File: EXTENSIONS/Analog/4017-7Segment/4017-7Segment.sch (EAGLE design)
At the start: 19 parts

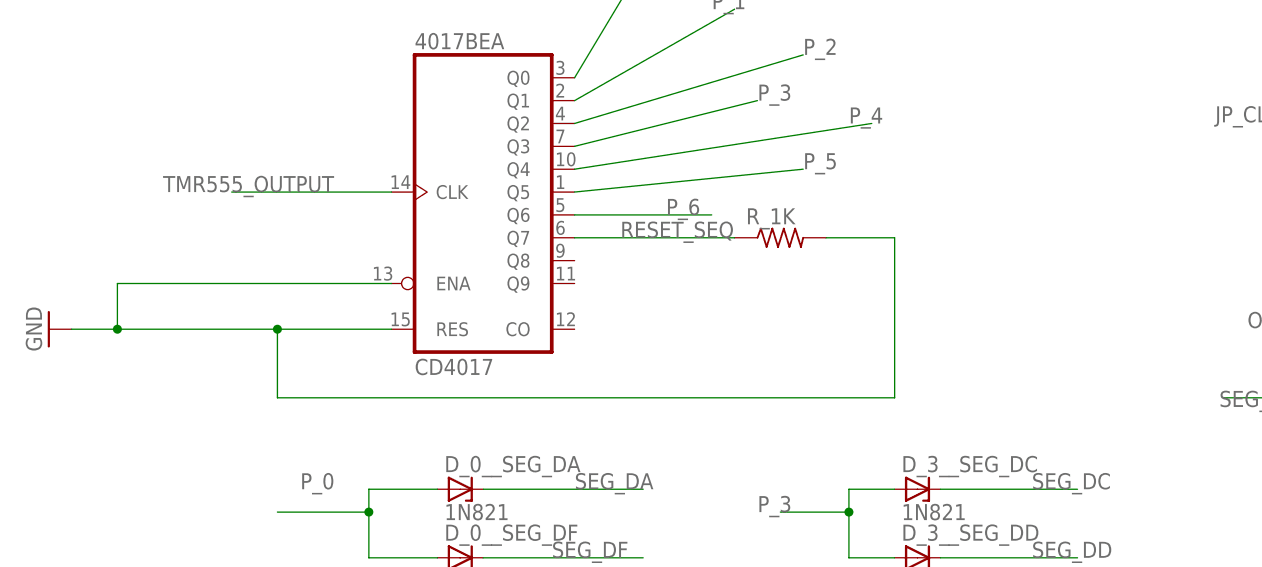
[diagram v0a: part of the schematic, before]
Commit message: Created 4017-7Segment v2
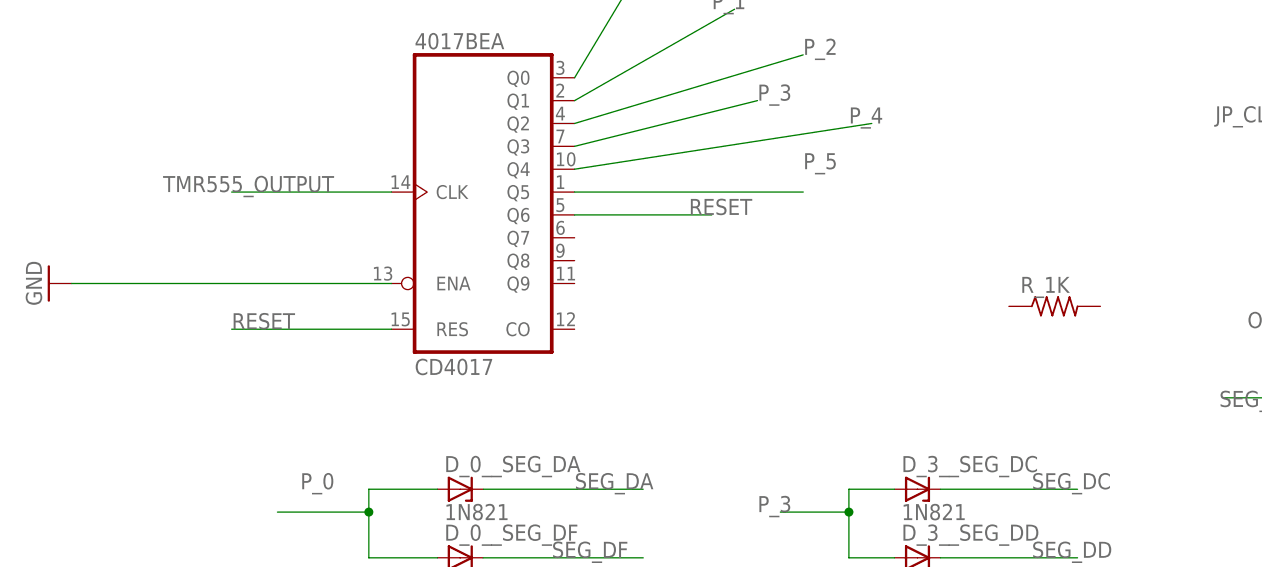
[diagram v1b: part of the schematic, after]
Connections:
- removed net P_6: 4017BEA.Q6
- removed net RESET_SEQ: 4017BEA.Q7, R_1K.1
- new net RESET: 4017BEA.Q6, 4017BEA.RES
- net GND: no longer 4017BEA.RES, R_1K.2
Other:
- moved on the sheet: R_1K
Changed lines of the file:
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@@
 <instance part="JP_CLOCK_IN" gate="A" x="17.78" y="127" rot="R180"/>
 <instance part="GND5" gate="1" x="45.72" y="121.92" rot="R90"/>
-<instance part="GND1" gate="1" x="-119.38" y="93.98" rot="R270"/>
+<instance part="GND1" gate="1" x="-119.38" y="99.06" rot="R270"/>
 <instance part="OUTPUTS" gate="A" x="17.78" y="104.14" rot="R180"/>
 <instance part="GND2" gate="1" x="43.18" y="99.06" rot="R90"/>
 <instance part="4017BE" gate="A" x="-71.12" y="109.22"/>
-<instance part="R_1K" gate="G$1" x="-38.1" y="104.14"/>
+<instance part="R_1K" gate="G$1" x="-7.62" y="96.52"/>
 <instance part="U$1" gate="G$1" x="76.2" y="76.2"/>
 <instance part="R_100O" gate="G$1" x="47.752" y="59.182"/>
@@
 </segment>
 <segment>
-<pinref part="GND1" gate="1" pin="GND"/>
-<wire x1="-116.84" y1="93.98" x2="-111.76" y2="93.98" width="0.1524" layer="91"/>
-<wire x1="-111.76" y1="93.98" x2="-111.76" y2="99.06" width="0.1524" layer="91"/>
-<pinref part="4017BE" gate="A" pin="ENA"/>
-<wire x1="-111.76" y1="99.06" x2="-81.28" y2="99.06" width="0.1524" layer="91"/>
-<pinref part="4017BE" gate="A" pin="RES"/>
-<wire x1="-81.28" y1="93.98" x2="-93.98" y2="93.98" width="0.1524" layer="91"/>
-<junction x="-111.76" y="93.98"/>
-<wire x1="-93.98" y1="93.98" x2="-111.76" y2="93.98" width="0.1524" layer="91"/>
-<wire x1="-93.98" y1="93.98" x2="-93.98" y2="86.36" width="0.1524" layer="91"/>
-<junction x="-93.98" y="93.98"/>
-<wire x1="-93.98" y1="86.36" x2="-25.4" y2="86.36" width="0.1524" layer="91"/>
-<wire x1="-25.4" y1="86.36" x2="-25.4" y2="104.14" width="0.1524" layer="91"/>
-<pinref part="R_1K" gate="G$1" pin="2"/>
-<wire x1="-25.4" y1="104.14" x2="-33.02" y2="104.14" width="0.1524" layer="91"/>
-</segment>
-<segment>
 <pinref part="GND3" gate="1" pin="GND"/>
 <pinref part="R_100O" gate="G$1" pin="1"/>
 <wire x1="35.052" y1="59.182" x2="42.672" y2="59.182" width="0.1524" layer="91"/>
+</segment>
+<segment>
+<pinref part="4017BE" gate="A" pin="ENA"/>
+<pinref part="GND1" gate="1" pin="GND"/>
+<wire x1="-81.28" y1="99.06" x2="-116.84" y2="99.06" width="0.1524" layer="91"/>
 </segment>
 </net>
@@
 <segment>
 <pinref part="4017BE" gate="A" pin="Q5"/>
-<wire x1="-60.96" y1="109.22" x2="-35.56" y2="111.76" width="0.1524" layer="91"/>
 <label x="-35.56" y="111.76" size="1.778" layer="95"/>
+<wire x1="-60.96" y1="109.22" x2="-35.56" y2="109.22" width="0.1524" layer="91"/>
 </segment>
 <segment>
@@
 </segment>
 </net>
-<net name="P_6" class="0">
+<net name="RESET" class="0">
+<segment>
+<pinref part="4017BE" gate="A" pin="RES"/>
+<wire x1="-81.28" y1="93.98" x2="-99.06" y2="93.98" width="0.1524" layer="91"/>
+<label x="-99.06" y="93.98" size="1.778" layer="95"/>
+</segment>
 <segment>
 <pinref part="4017BE" gate="A" pin="Q6"/>
 <wire x1="-60.96" y1="106.68" x2="-45.72" y2="106.68" width="0.1524" layer="91"/>
-<label x="-50.8" y="106.68" size="1.778" layer="95"/>
-</segment>
-</net>
-<net name="RESET_SEQ" class="0">
-<segment>
-<pinref part="4017BE" gate="A" pin="Q7"/>
-<pinref part="R_1K" gate="G$1" pin="1"/>
-<wire x1="-60.96" y1="104.14" x2="-43.18" y2="104.14" width="0.1524" layer="91"/>
-<label x="-55.88" y="104.14" size="1.778" layer="95"/>
-</segment>
-</net>
+<label x="-48.26" y="106.68" size="1.778" layer="95"/>
+</segment>
+</net>

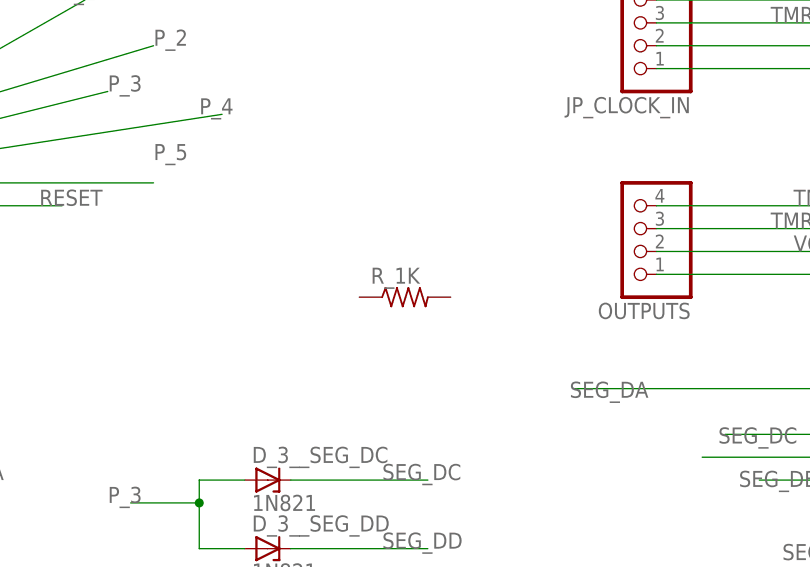
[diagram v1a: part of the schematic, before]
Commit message: Created 4017-7Segment v2
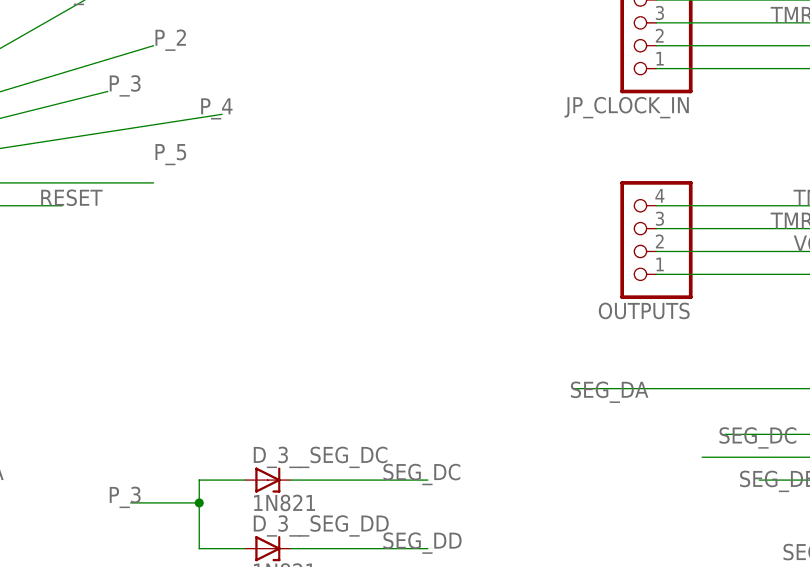
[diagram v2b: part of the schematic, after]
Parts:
- removed R_1K: (no value), adafruit:R-US_R1206
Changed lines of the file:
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@@
 <part name="GND2" library="supply1" deviceset="GND" device=""/>
 <part name="4017BE" library="SparkFun-DigitalIC" deviceset="CD4017" device="" value="CD4017"/>
-<part name="R_1K" library="adafruit" deviceset="R-US_" device="R1206"/>
 <part name="U$1" library="SparkFun-Displays" deviceset="7-SEGMENT-DISPLAY" device="PTH"/>
 <part name="R_100O" library="adafruit" deviceset="R-US_" device="R1206"/>
@@
 <instance part="GND2" gate="1" x="43.18" y="99.06" rot="R90"/>
 <instance part="4017BE" gate="A" x="-71.12" y="109.22"/>
-<instance part="R_1K" gate="G$1" x="-7.62" y="96.52"/>
 <instance part="U$1" gate="G$1" x="76.2" y="76.2"/>
 <instance part="R_100O" gate="G$1" x="47.752" y="59.182"/>
